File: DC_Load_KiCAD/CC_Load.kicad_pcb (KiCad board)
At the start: 2 copper layers, 90 x 60 mm, 99 parts, among them J1 CONN_V_SENSE, J10 CONN_LED, J11 CONN_ICSP, J12 CONN_PINS, J2 CONN_FAN, J3 CONN_PWR, J4 CONN_PWR_LED, J5 USBC_CONN, J6 CONN_NTC, J7 CONN_LOAD, J8 CONN_ENCODER, J9 CONN_OLED, Q1 2N7002, Q2 IRLZ44N, Q3 IRLZ44N, Q4 IRLZ44N, Q5 IRLZ44N, Q6 IRLZ44N, SW1 RST_BTN, U1 LM7805_TO220, U2 OPA4376, U3 CH340C, U4 ATmega328P-A, U5 ADC (INA219AIDR), U6 DAC (MCP4716A0T-E/CH), U7 ADR5040BRTZ, Y1 16MHz

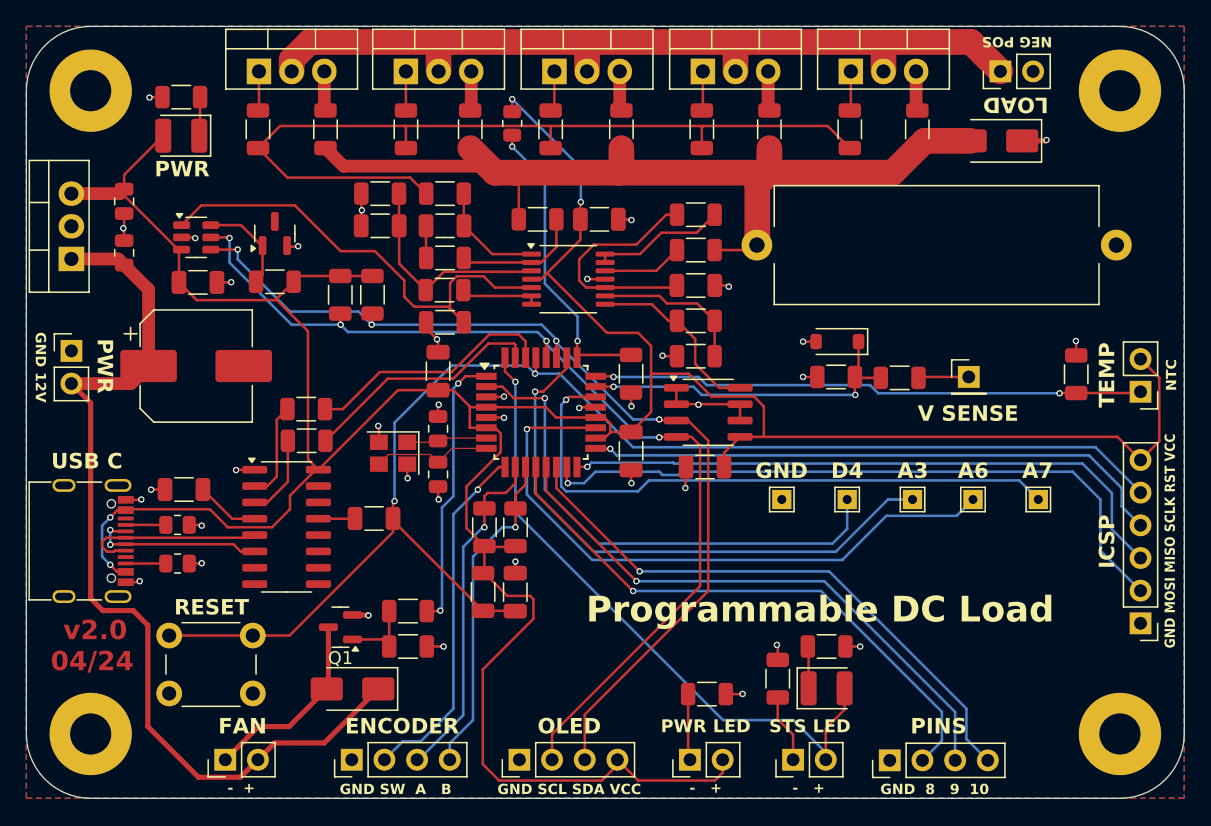
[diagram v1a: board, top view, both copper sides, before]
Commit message: Update PCB to ver 3.0, in code updatet drivers a bit
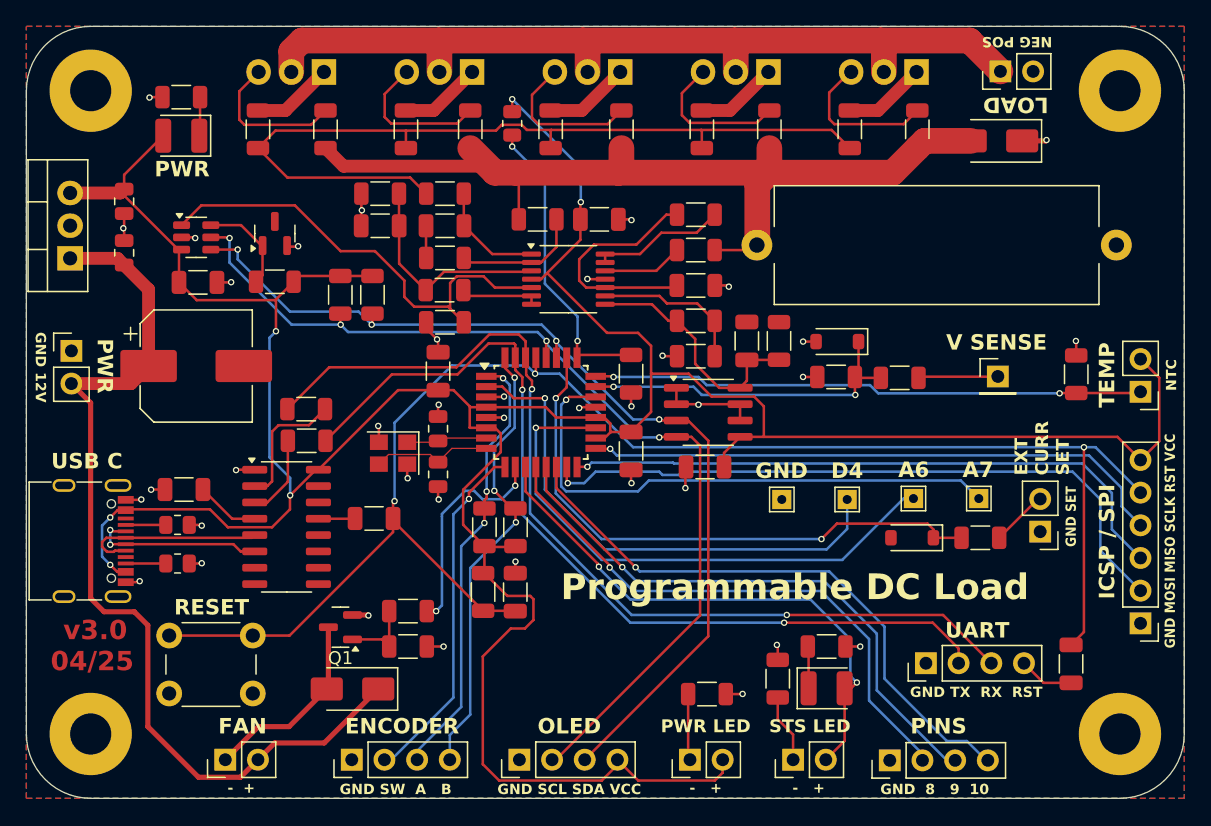
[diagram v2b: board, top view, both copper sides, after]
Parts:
- removed the TP3 at (158.9, 96.8)
- added C16: 100n, Capacitor_SMD:C_1206_3216Metric, F.Cu at (146.0, 84.5)
- added C18: 100n, Capacitor_SMD:C_1206_3216Metric, F.Cu at (171.2, 109.5)
- added D6: 5V, Diode_SMD:D_SOD-123, F.Cu at (158.8, 99.8)
- added J11: CONN_UART, Connector_PinHeader_2.54mm:PinHeader_1x04_P2.54mm_Vertical, F.Cu at (159.9, 109.5)
- added J14: CONN_EXT_CURR_SET, Connector_PinHeader_2.54mm:PinHeader_1x02_P2.54mm_Vertical, F.Cu at (168.8, 99.3)
- added R38: 100k, Resistor_SMD:R_1206_3216Metric, F.Cu at (148.5, 84.5)
- added R42: 10k, Resistor_SMD:R_1206_3216Metric, F.Cu at (164.2, 99.8)
- C13, C14: value 10p -> 20p
- J12: renamed from J11; value CONN_ICSP -> CONN_ICSP_SPI
- J5: value USBC_CONN -> CONN_USBC
- Q2, Q3, Q4, Q5, Q6: moved to B.Cu
- R2, R4: value 470R -> 0R
- moved Q3 5.15 mm to (124.6, 63.5), turned to 180 degrees
- moved Q4 5.12 mm to (136.2, 63.5), turned to 180 degrees
- moved Q6 5.11 mm to (159.2, 63.5), turned to 180 degrees
- moved Q5 5.10 mm to (147.7, 63.5), turned to 180 degrees
- moved Q2 5.05 mm to (113.1, 63.5), turned to 180 degrees
- moved TP1 4.63 mm to (158.9, 96.7)
- moved TP2 4.63 mm to (164.0, 96.7)
- moved J1 2.26 mm to (165.5, 87.2)
- moved U1 0.11 mm to (93.4, 78.0)
- turned R2 to 0 degrees
- renumbered C16 to C17, J12 to J13, R18 to R16, R16 to R17, R17 to R18, R38 to R39, R39 to R40, R40 to R43, R9 to R8, R8 to R9, TP4 to TP3, TP5 to TP4
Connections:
- net SHUNT_TEMP_UC renamed PCB_TEMP_UC
- U4 pad 1: FAN_OUT -> ENCODER_B
- U4 pad 10: ENCODER_B -> FAN_OUT
- U4 pad 11: ENCODER_A -> LED_OUT
- U4 pad 26: /ADC_03 -> EXT_CURR_SET_UC
- U4 pad 32: LED_OUT -> ENCODER_A
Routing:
- net RXD_UC: track 19.5 -> 75.5 mm, vias 0 -> 2
- net TXD_UC: track 18.9 -> 70.7 mm, vias 0 -> 2
- net EXT_CURR_SET_UC: track 0.00 -> 45.2 mm, vias 0 -> 2
- net /ADC_03: track 44.8 -> 0.00 mm, vias 1 -> 0
- net RST_UC: track 107.1 -> 122.8 mm, vias 2 -> 3
- net ENCODER_A: track 25.8 -> 35.2 mm, vias 1 -> 3
- net Net-(Q6-S): track 3.07 -> 11.9 mm
- net Net-(Q4-S): track 3.09 -> 11.9 mm
- net Net-(Q2-S): track 3.07 -> 11.7 mm
- net Net-(Q3-S): track 3.07 -> 11.5 mm
- net Net-(Q5-S): track 3.07 -> 11.5 mm
- net LED_OUT: track 51.0 -> 42.9 mm, vias 1 -> 2
- net ENCODER_B: track 26.9 -> 34.2 mm, vias 1 -> 3
- net /ADC_06: track 49.2 -> 43.2 mm
- net /CURR_SENSE_UC: track 14.3 -> 19.2 mm
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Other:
- board text added: "04/25"
- board text added: "EXT CURR SET"
- board text added: "GND SET"
- board text added: "GND TX RX RST"
- board text added: "ICSP / SPI"
- board text added: "UART"
- board text added: "v3.0"
- board text removed: "04/24"
- board text removed: "A3"
- board text removed: "ICSP"
- board text removed: "v2.0"
